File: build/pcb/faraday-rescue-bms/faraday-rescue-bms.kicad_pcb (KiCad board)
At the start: 4 copper layers, 481.3 x 23.7 mm, 155 parts, among them J1 532610571, J3 532610471, Q1 FCX495TA, Q3 2N7002, U1 BQ7697202, U2 STM32L010K8Tx, U4 THVD2410DR, Y1 ABS07-32.768KHZ-T

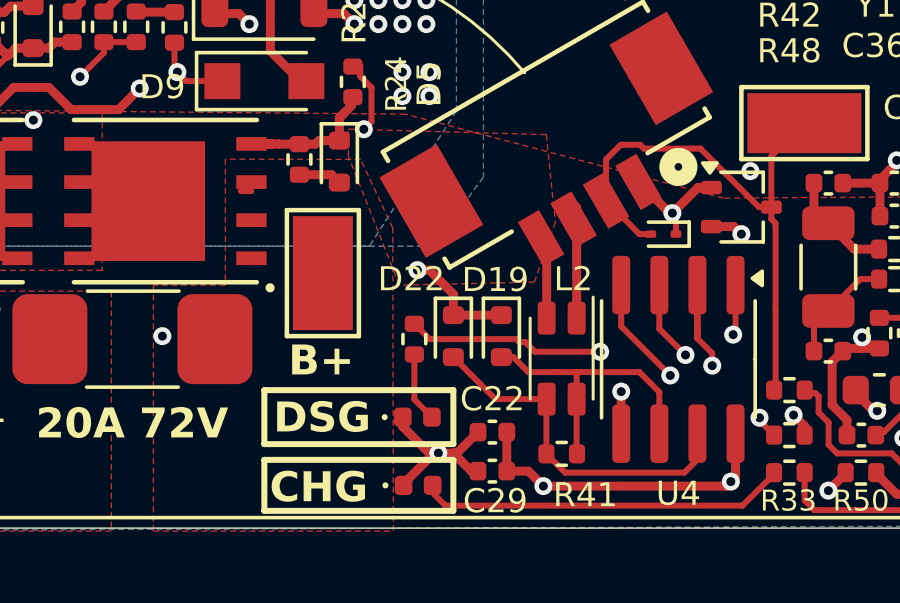
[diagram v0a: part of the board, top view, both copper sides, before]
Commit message: Rotated diodes to fix only hardware issue.
D19 and D22 were flipped on the schematic and this propagated to the PCB. All boards from round 2 needed to be reworked to rotate D19 and D22 180deg.
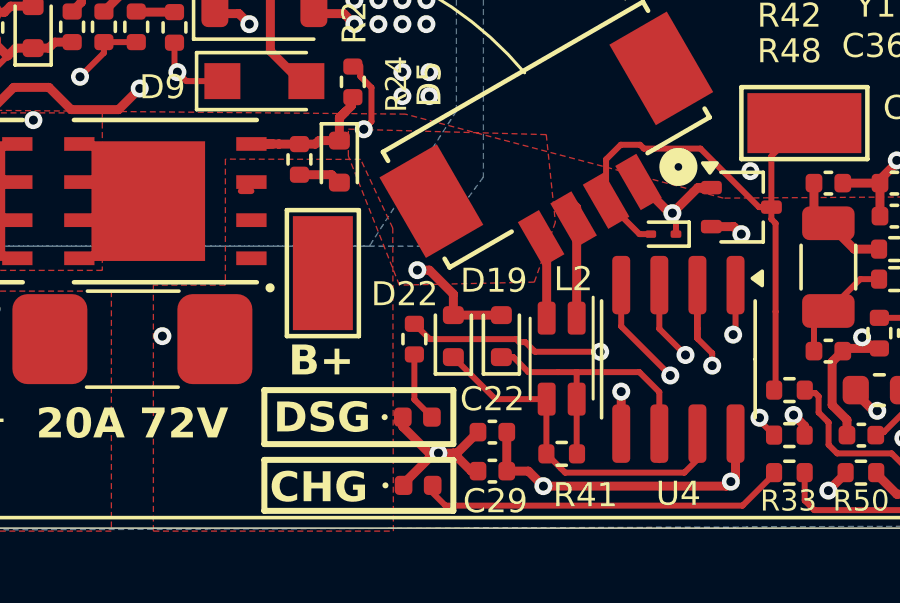
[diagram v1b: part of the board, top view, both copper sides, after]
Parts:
- C13, C24: value 100nF -> 100nF 100V
- C22, C30, C33, C37: value 10u -> 10u 6.3V
- C26, C29, C31, C32, C34: value 100nF -> 100nF 6.3V
- C27: value 1uF -> 1uF 6.3V
- C39: value 22nF -> 22nF 50V
- C40: value 1uF -> 1uF 100V
- C41, C42: value 1uF -> 1uF 25V
- F2: value BEL Fuse 0ZCJ0005FF2E 50mA 60VDC -> BEL Fuse 0ZCJ0005FF2E
- R15, R16, R19, R22, R41, R43, R44: value 120 -> 120R
- R39, R45, R46: value 330 -> 330R
- turned D19 to 90 degrees
- turned D22 to 90 degrees
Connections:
- D19 pad 1: VSS -> Net-(D19-A1)
- D19 pad 2: Net-(D19-A2) -> VSS
- D22 pad 1: VSS -> Net-(D22-A1)
- D22 pad 2: Net-(D22-A2) -> VSS
- J1 pad 7: Net-(BT1-+-Pad3) -> (no net)
- L2 pad 2: Net-(D19-A2) -> Net-(D19-A1)
- L2 pad 3: Net-(D22-A2) -> Net-(D22-A1)
- R41 pad 1: Net-(D19-A2) -> Net-(D19-A1)
- R41 pad 2: Net-(D22-A2) -> Net-(D22-A1)
- U4 pad 6: Net-(D19-A2) -> Net-(D19-A1)
- U4 pad 7: Net-(D22-A2) -> Net-(D22-A1)
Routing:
- net Net-(D19-A2): track 12.3 -> 0.00 mm
- net Net-(D19-A1): track 0.00 -> 12.3 mm
- net Net-(D22-A2): track 11.6 -> 0.00 mm
- net Net-(D22-A1): track 0.00 -> 11.6 mm
